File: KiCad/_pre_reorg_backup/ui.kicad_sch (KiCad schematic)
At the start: 12 parts, among them U12 LM35, U7 SN74AHCT244DBR

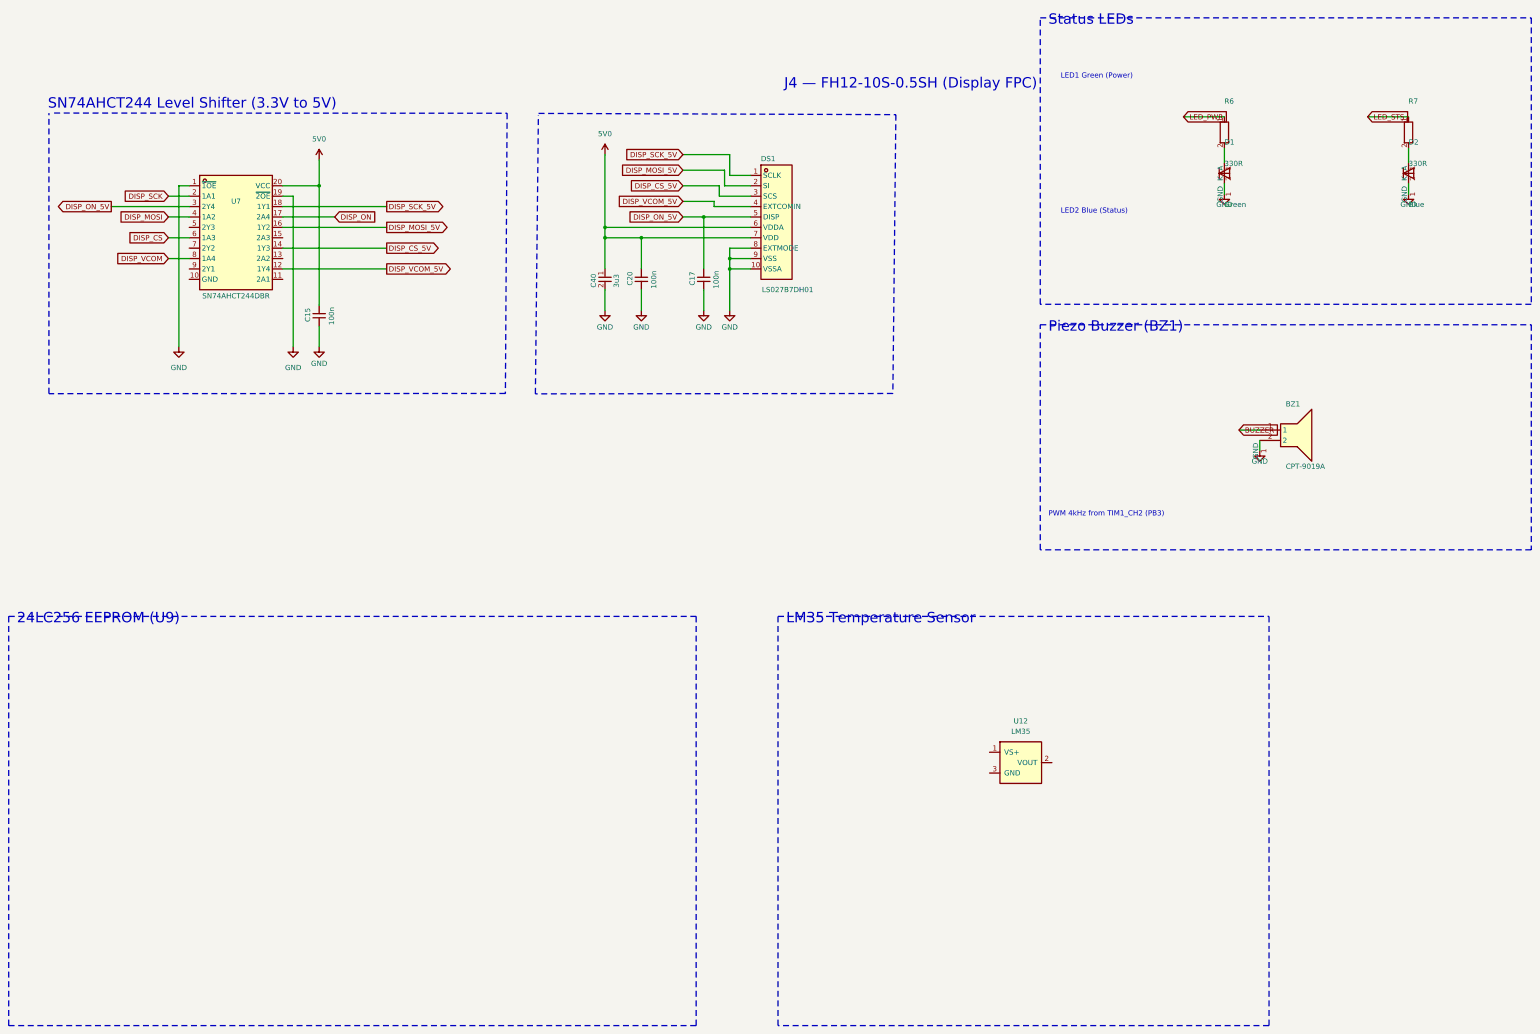
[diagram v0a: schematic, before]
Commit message: Schematics edited manually
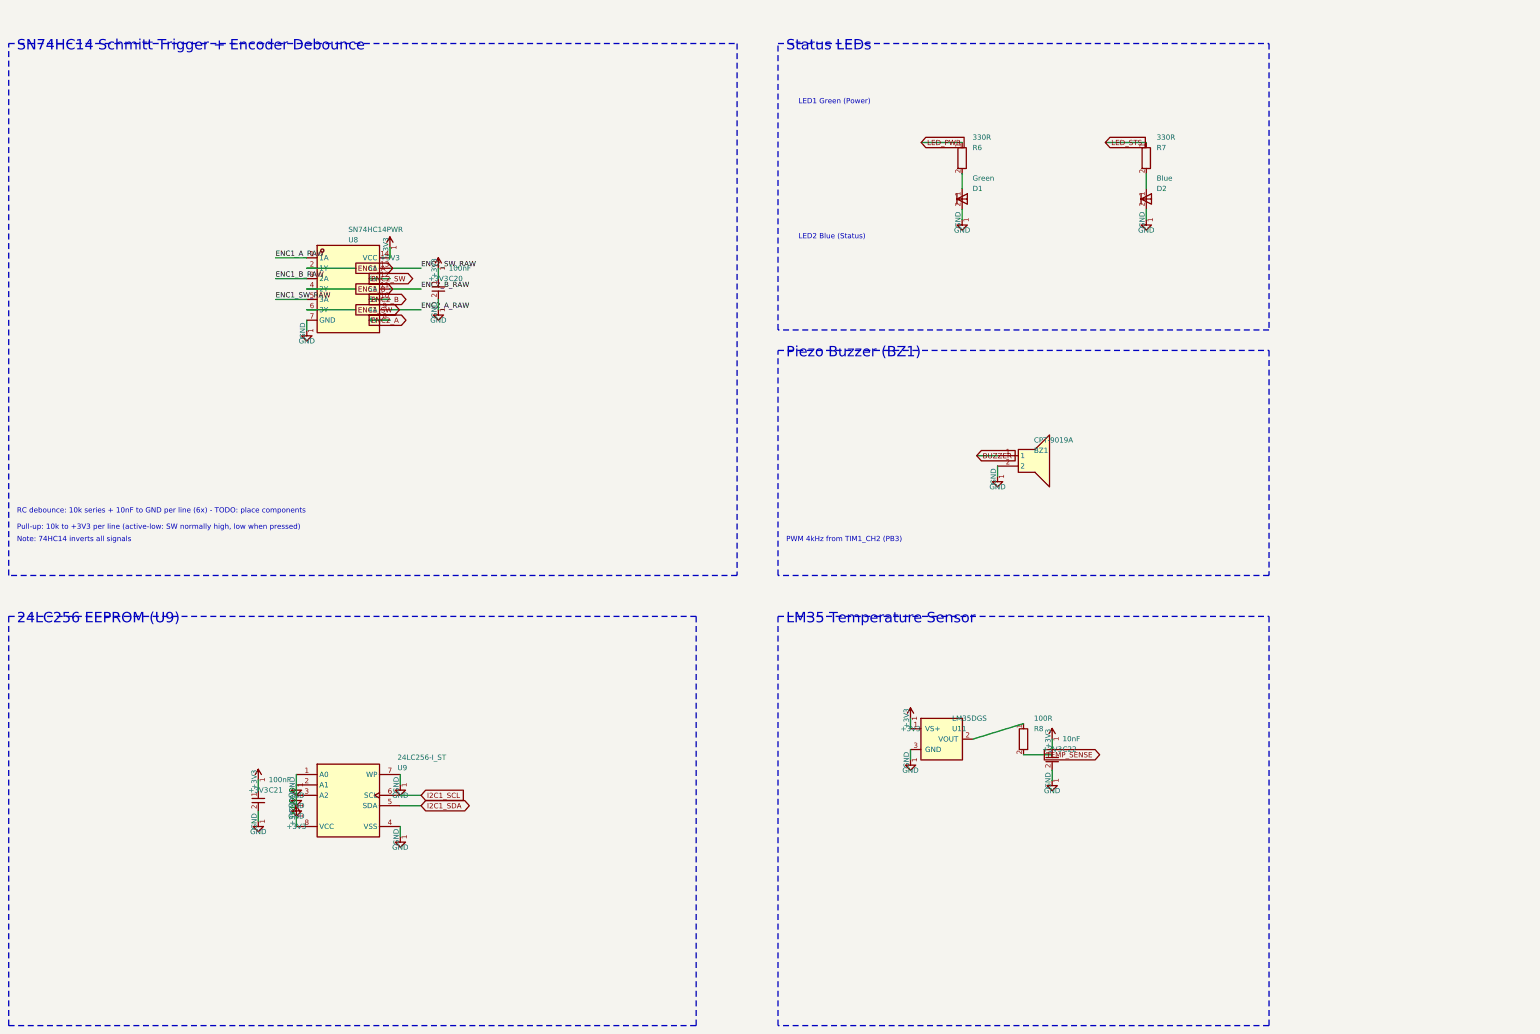
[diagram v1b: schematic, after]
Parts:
- removed C15, C17: 100n, sldrnrd:C_0603, symbol sldrnrd:Capacitor/C_0603
- removed C40: 3u3, sldrnrd:C_0805, symbol sldrnrd:Capacitor/C_0805
- removed DS1: LS027B7DH01, sldrnrd:FPC-10-1.5, symbol sldrnrd:Display/LS027B7DH01
- removed U12: LM35, sldrnrd:SOT-23, symbol sldrnrd:Sensor/LM35
- removed U7: SN74AHCT244DBR, sldrnrd:SSOP-20, symbol sldrnrd:Logic/74/SN74AHCT244DBR
- added C21: 100nF, sldrnrd:C_0603, symbol sldrnrd:Capacitor/C_0603
- added C22: 10nF, sldrnrd:C_0603, symbol sldrnrd:Capacitor/C_0603
- added R8: 100R, sldrnrd:R_0603, symbol sldrnrd:Resistor/R_0603
- added U11: LM35DGS, sldrnrd:SOT-23, symbol sldrnrd:Sensor/LM35
- added U8: SN74HC14PWR, sldrnrd:TSSOP-14, symbol sldrnrd:Logic/74/SN74HC14PWR
- added U9: 24LC256-I_ST, sldrnrd:TSSOP-8, symbol sldrnrd:Memory/EEPROM/24LC256-I_ST
- C20: value 100n -> 100nF
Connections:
- net GND: now also C21.2, C22.2, U11.3 (GND), U8.7 (GND), U9.1 (A0), U9.2 (A1), U9.3 (A2), U9.4 (VSS), U9.7 (WP)
- net 5V0 renamed +3V3
- net +3V3: now also C21.1, C22.1, U11.1 (VS+), U8.14 (VCC), U9.8 (VCC)
- new net: R8.1, U11.2 (VOUT)
- new net ENC1_A: U8.2 (1Y)
- new net ENC1_A_RAW: U8.1 (1A)
- new net ENC1_B: U8.4 (2Y)
- new net ENC1_B_RAW: U8.3 (2A)
- new net ENC1_SW: U8.6 (3Y)
- new net ENC1_SW_RAW: U8.5 (3A)
- new net ENC2_A: U8.8 (4Y)
- new net ENC2_A_RAW: U8.9 (4A)
- new net ENC2_B: U8.10 (5Y)
- new net ENC2_B_RAW: U8.11 (5A)
- new net ENC2_SW: U8.12 (6Y)
- new net ENC2_SW_RAW: U8.13 (6A)
- new net I2C1_SCL: U9.6 (SCL)
- new net I2C1_SDA: U9.5 (SDA)
- new net TEMP_SENSE: R8.2
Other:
- note added: "Note: 74HC14 inverts all signals"
- note added: "Pull-up: 10k to +3V3 per line (active-low: SW normally high, low when pressed)"
- note added: "RC debounce: 10k series + 10nF to GND per line (6x) - TODO: place components"
- note added: "SN74HC14 Schmitt Trigger + Encoder Debounce"
- note removed: "J4 — FH12-10S-0.5SH (Display FPC)"
- note removed: "SN74AHCT244 Level Shifter (3.3V to 5V)"
- moved on the sheet: BZ1, R6, R7
